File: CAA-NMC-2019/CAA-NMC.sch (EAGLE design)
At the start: 147 parts, among them IC1 ATTINY85-20SU, J1 M20-9980346

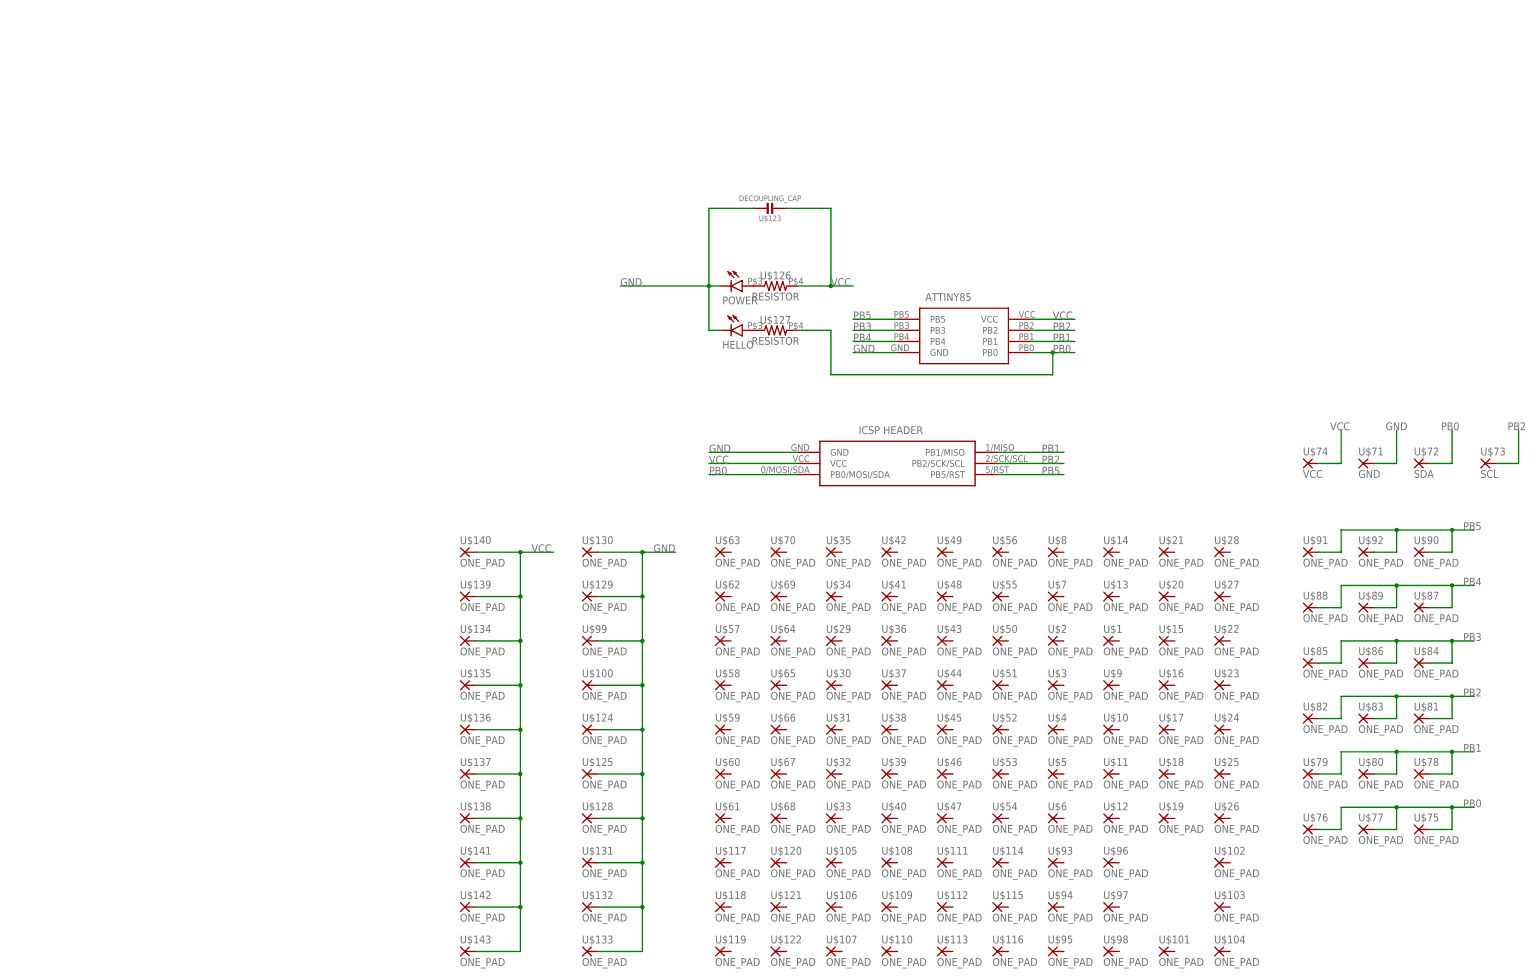
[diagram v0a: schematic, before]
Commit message: added smt battery mount
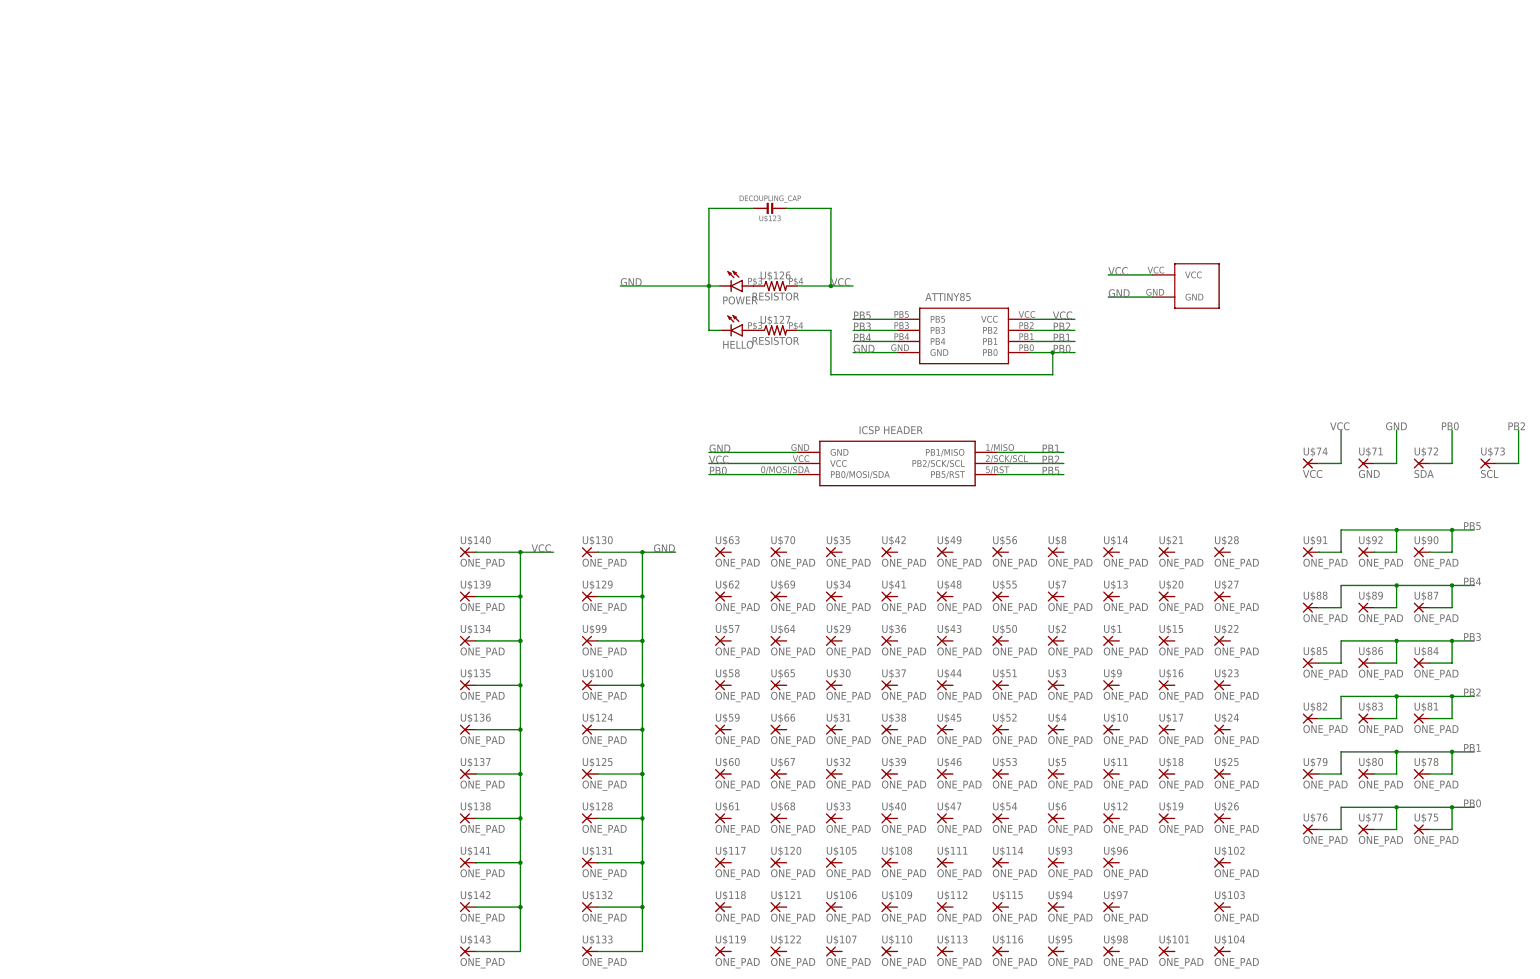
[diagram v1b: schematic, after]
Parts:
- added U$144: SMT-BATTERY-HOLDER, BadgeParts:SMT-BATTERY-HOLDER
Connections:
- net GND: now also U$144.GND
- net VCC: now also U$144.VCC

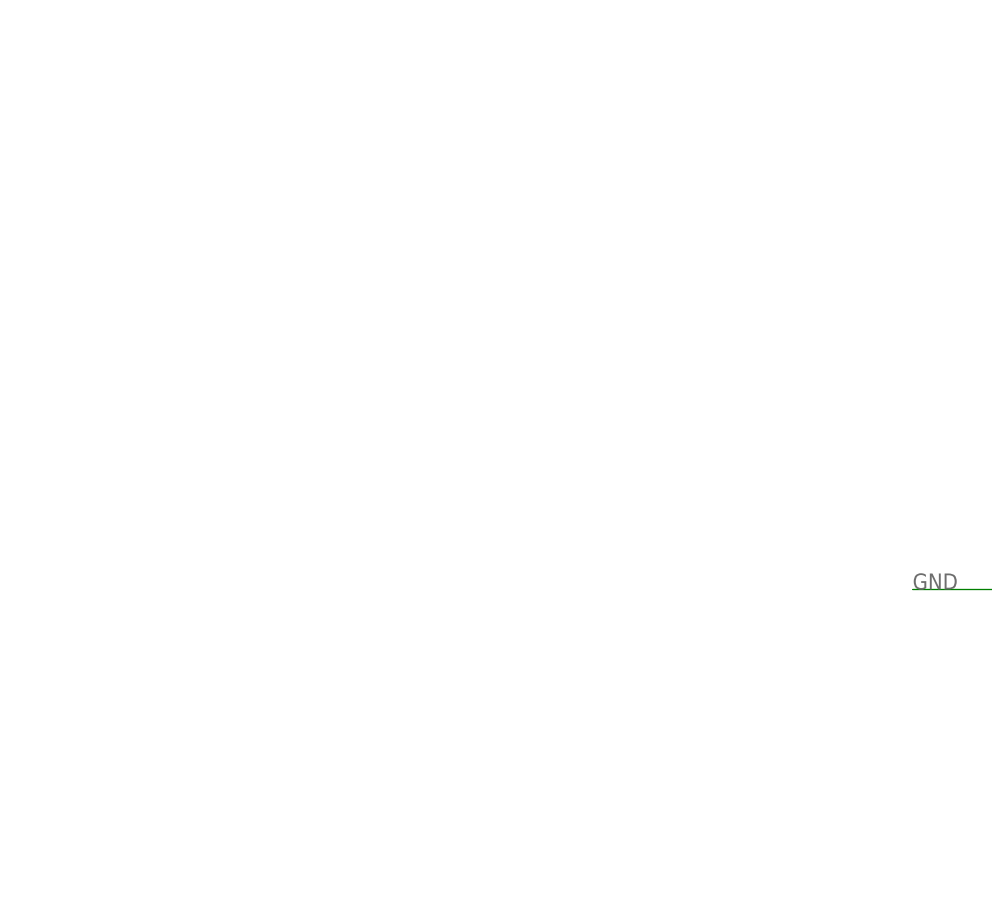
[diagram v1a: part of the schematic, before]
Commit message: added lanyard hole, 3 RGB LEDs
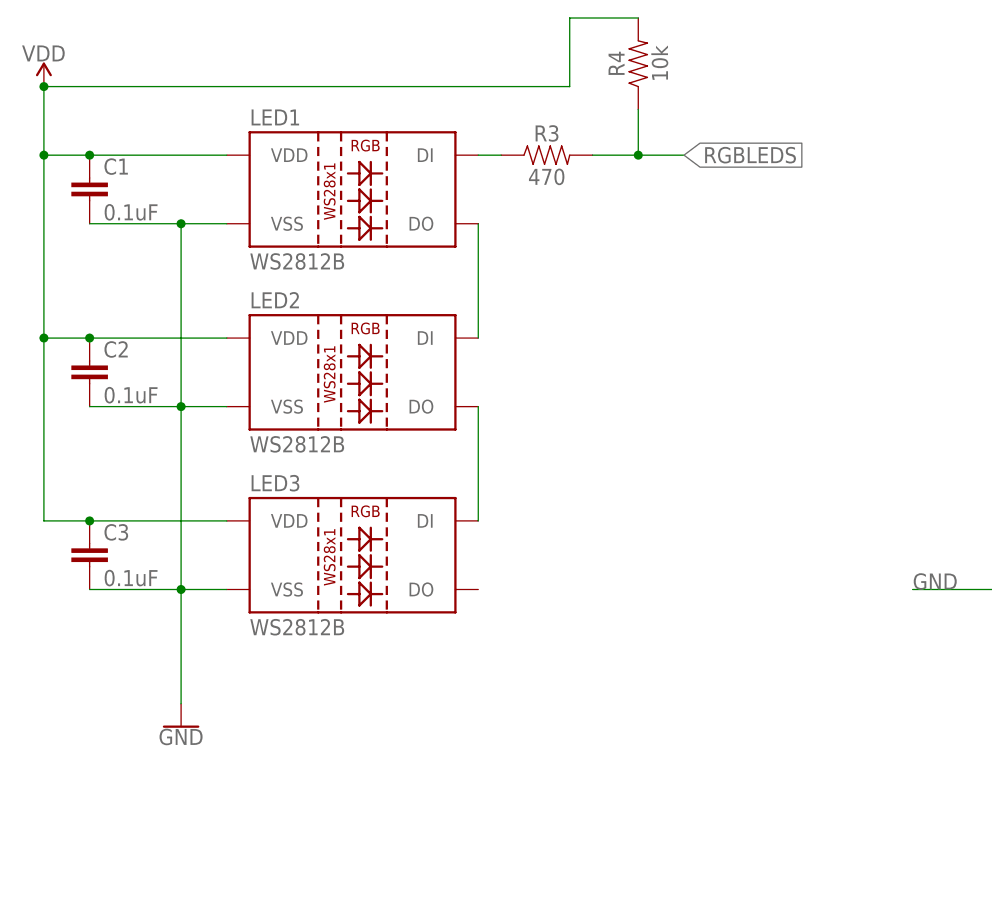
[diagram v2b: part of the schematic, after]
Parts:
- added C1, C2, C3: 0.1uF, SparkFun-Capacitors:0.1UF-0603-25V-5%
- added LED1, LED2, LED3: WS2812B, SparkFun-LED:WS2812B
- added R3: 470, SparkFun-Resistors:470OHM-0603-1/10W-1%
- added R4: 10k, SparkFun-Resistors:10KOHM-0603-1/10W-1%
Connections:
- new net N$10: LED2.DO, LED3.DI
- new net N$12: LED1.DI, R3.1
- new net N$9: LED1.DO, LED2.DI
- new net RGBLEDS: R3.2, R4.1
- new net VDD: C1.1, C2.1, C3.1, LED1.VDD, LED2.VDD, LED3.VDD, R4.2
- net GND: now also C1.2, C2.2, C3.2, LED1.VSS, LED2.VSS, LED3.VSS
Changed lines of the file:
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@@
 <part name="U$143" library="BadgeParts" deviceset="ONE_PAD" device=""/>
 <part name="U$144" library="BadgeParts" deviceset="SMT-BATTERY-HOLDER" device=""/>
+<part name="LED1" library="SparkFun-LED" library_urn="urn:adsk.eagle:library:529" deviceset="WS2812B" device="" package3d_urn="urn:adsk.eagle:package:39369/1" value="WS2812B"/>
+<part name="SUPPLY5" library="SparkFun-PowerSymbols" library_urn="urn:adsk.eagle:library:530" deviceset="VDD" device=""/>
+<part name="LED2" library="SparkFun-LED" library_urn="urn:adsk.eagle:library:529" deviceset="WS2812B" device="" package3d_urn="urn:adsk.eagle:package:39369/1" value="WS2812B"/>
+<part name="LED3" library="SparkFun-LED" library_urn="urn:adsk.eagle:library:529" deviceset="WS2812B" device="" package3d_urn="urn:adsk.eagle:package:39369/1" value="WS2812B"/>
+<part name="C1" library="SparkFun-Capacitors" library_urn="urn:adsk.eagle:library:510" deviceset="0.1UF" device="-0603-25V-5%" package3d_urn="urn:adsk.eagle:package:37414/1" value="0.1uF"/>
+<part name="C2" library="SparkFun-Capacitors" library_urn="urn:adsk.eagle:library:510" deviceset="0.1UF" device="-0603-25V-5%" package3d_urn="urn:adsk.eagle:package:37414/1" value="0.1uF"/>
+<part name="C3" library="SparkFun-Capacitors" library_urn="urn:adsk.eagle:library:510" deviceset="0.1UF" device="-0603-25V-5%" package3d_urn="urn:adsk.eagle:package:37414/1" value="0.1uF"/>
+<part name="R3" library="SparkFun-Resistors" library_urn="urn:adsk.eagle:library:532" deviceset="470OHM" device="-0603-1/10W-1%" package3d_urn="urn:adsk.eagle:package:39650/1" value="470"/>
+<part name="R4" library="SparkFun-Resistors" library_urn="urn:adsk.eagle:library:532" deviceset="10KOHM" device="-0603-1/10W-1%" package3d_urn="urn:adsk.eagle:package:39650/1" value="10k"/>
+<part name="GND5" library="SparkFun-PowerSymbols" library_urn="urn:adsk.eagle:library:530" deviceset="GND" device=""/>
 </parts>
 <sheets>
@@
 </instance>
 <instance part="U$144" gate="G$1" x="-55.88" y="76.2" smashed="yes"/>
+<instance part="LED1" gate="G$1" x="-243.84" y="116.84" smashed="yes">
+<attribute name="NAME" x="-256.54" y="125.222" size="1.778" layer="95"/>
+<attribute name="VALUE" x="-256.54" y="109.22" size="1.778" layer="95"/>
+</instance>
+<instance part="SUPPLY5" gate="VDD" x="-279.4" y="129.54" smashed="yes">
+<attribute name="VALUE" x="-279.4" y="132.334" size="1.778" layer="96" align="bottom-center"/>
+</instance>
+<instance part="LED2" gate="G$1" x="-243.84" y="96.52" smashed="yes">
+<attribute name="NAME" x="-256.54" y="104.902" size="1.778" layer="95"/>
+<attribute name="VALUE" x="-256.54" y="88.9" size="1.778" layer="95"/>
+</instance>
+<instance part="LED3" gate="G$1" x="-243.84" y="76.2" smashed="yes">
+<attribute name="NAME" x="-256.54" y="84.582" size="1.778" layer="95"/>
+<attribute name="VALUE" x="-256.54" y="68.58" size="1.778" layer="95"/>
+</instance>
+<instance part="C1" gate="G$1" x="-274.32" y="116.84" smashed="yes">
+<attribute name="NAME" x="-272.796" y="119.761" size="1.778" layer="95" font="vector"/>
+<attribute name="VALUE" x="-272.796" y="114.681" size="1.778" layer="96" font="vector"/>
+</instance>
+<instance part="C2" gate="G$1" x="-274.32" y="96.52" smashed="yes">
+<attribute name="NAME" x="-272.796" y="99.441" size="1.778" layer="95" font="vector"/>
+<attribute name="VALUE" x="-272.796" y="94.361" size="1.778" layer="96" font="vector"/>
+</instance>
+<instance part="C3" gate="G$1" x="-274.32" y="76.2" smashed="yes">
+<attribute name="NAME" x="-272.796" y="79.121" size="1.778" layer="95" font="vector"/>
+<attribute name="VALUE" x="-272.796" y="74.041" size="1.778" layer="96" font="vector"/>
+</instance>
+<instance part="R3" gate="G$1" x="-223.52" y="121.92" smashed="yes">
+<attribute name="NAME" x="-223.52" y="123.444" size="1.778" layer="95" font="vector" align="bottom-center"/>
+<attribute name="VALUE" x="-223.52" y="120.396" size="1.778" layer="96" font="vector" align="top-center"/>
+</instance>
+<instance part="R4" gate="G$1" x="-213.36" y="132.08" smashed="yes" rot="R90">
+<attribute name="NAME" x="-214.884" y="132.08" size="1.778" layer="95" font="vector" rot="R90" align="bottom-center"/>
+<attribute name="VALUE" x="-211.836" y="132.08" size="1.778" layer="96" font="vector" rot="R90" align="top-center"/>
+</instance>
+<instance part="GND5" gate="1" x="-264.16" y="58.42" smashed="yes">
+<attribute name="VALUE" x="-264.16" y="58.166" size="1.778" layer="96" align="top-center"/>
+</instance>
 </instances>
 <busses>
@@
 <label x="-71.12" y="71.12" size="1.778" layer="95"/>
 </segment>
+<segment>
+<pinref part="LED3" gate="G$1" pin="VSS"/>
+<pinref part="C3" gate="G$1" pin="2"/>
+<wire x1="-259.08" y1="73.66" x2="-264.16" y2="73.66" width="0.1524" layer="91"/>
+<wire x1="-264.16" y1="73.66" x2="-274.32" y2="73.66" width="0.1524" layer="91"/>
+<junction x="-264.16" y="73.66"/>
+<pinref part="LED2" gate="G$1" pin="VSS"/>
+<pinref part="C2" gate="G$1" pin="2"/>
+<wire x1="-259.08" y1="93.98" x2="-264.16" y2="93.98" width="0.1524" layer="91"/>
+<wire x1="-264.16" y1="93.98" x2="-274.32" y2="93.98" width="0.1524" layer="91"/>
+<wire x1="-264.16" y1="73.66" x2="-264.16" y2="93.98" width="0.1524" layer="91"/>
+<junction x="-264.16" y="93.98"/>
+<pinref part="LED1" gate="G$1" pin="VSS"/>
+<pinref part="C1" gate="G$1" pin="2"/>
+<wire x1="-259.08" y1="114.3" x2="-264.16" y2="114.3" width="0.1524" layer="91"/>
+<wire x1="-264.16" y1="114.3" x2="-274.32" y2="114.3" width="0.1524" layer="91"/>
+<wire x1="-264.16" y1="93.98" x2="-264.16" y2="114.3" width="0.1524" layer="91"/>
+<junction x="-264.16" y="114.3"/>
+<pinref part="GND5" gate="1" pin="GND"/>
+<wire x1="-264.16" y1="73.66" x2="-264.16" y2="60.96" width="0.1524" layer="91"/>
+</segment>
 </net>
 <net name="PB2" class="0">
@@
 </segment>
 </net>
+<net name="VDD" class="1">
+<segment>
+<pinref part="LED1" gate="G$1" pin="VDD"/>
+<pinref part="C1" gate="G$1" pin="1"/>
+<wire x1="-259.08" y1="121.92" x2="-274.32" y2="121.92" width="0.1524" layer="91"/>
+<pinref part="SUPPLY5" gate="VDD" pin="VDD"/>
+<wire x1="-274.32" y1="121.92" x2="-279.4" y2="121.92" width="0.1524" layer="91"/>
+<wire x1="-279.4" y1="121.92" x2="-279.4" y2="129.54" width="0.1524" layer="91"/>
+<junction x="-274.32" y="121.92"/>
+<pinref part="LED2" gate="G$1" pin="VDD"/>
+<pinref part="C2" gate="G$1" pin="1"/>
+<wire x1="-259.08" y1="101.6" x2="-274.32" y2="101.6" width="0.1524" layer="91"/>
+<wire x1="-274.32" y1="101.6" x2="-279.4" y2="101.6" width="0.1524" layer="91"/>
+<wire x1="-279.4" y1="101.6" x2="-279.4" y2="121.92" width="0.1524" layer="91"/>
+<junction x="-274.32" y="101.6"/>
+<junction x="-279.4" y="121.92"/>
+<pinref part="LED3" gate="G$1" pin="VDD"/>
+<pinref part="C3" gate="G$1" pin="1"/>
+<wire x1="-259.08" y1="81.28" x2="-274.32" y2="81.28" width="0.1524" layer="91"/>
+<wire x1="-274.32" y1="81.28" x2="-279.4" y2="81.28" width="0.1524" layer="91"/>
+<wire x1="-279.4" y1="81.28" x2="-279.4" y2="101.6" width="0.1524" layer="91"/>
+<junction x="-274.32" y="81.28"/>
+<junction x="-279.4" y="101.6"/>
+<wire x1="-279.4" y1="129.54" x2="-220.98" y2="129.54" width="0.1524" layer="91"/>
+<junction x="-279.4" y="129.54"/>
+<wire x1="-220.98" y1="129.54" x2="-220.98" y2="137.16" width="0.1524" layer="91"/>
+<pinref part="R4" gate="G$1" pin="2"/>
+<wire x1="-220.98" y1="137.16" x2="-213.36" y2="137.16" width="0.1524" layer="91"/>
+</segment>
+</net>
+<net name="RGBLEDS" class="0">
+<segment>
+<pinref part="R3" gate="G$1" pin="2"/>
+<wire x1="-218.44" y1="121.92" x2="-213.36" y2="121.92" width="0.1524" layer="91"/>
+<pinref part="R4" gate="G$1" pin="1"/>
+<wire x1="-213.36" y1="127" x2="-213.36" y2="121.92" width="0.1524" layer="91"/>
+<wire x1="-213.36" y1="121.92" x2="-208.28" y2="121.92" width="0.1524" layer="91"/>
+<junction x="-213.36" y="121.92"/>
+<label x="-208.28" y="121.92" size="1.778" layer="95" xref="yes"/>
+</segment>
+</net>
+<net name="N$9" class="0">
+<segment>
+<pinref part="LED1" gate="G$1" pin="DO"/>
+<pinref part="LED2" gate="G$1" pin="DI"/>
+<wire x1="-231.14" y1="114.3" x2="-231.14" y2="101.6" width="0.1524" layer="91"/>
+</segment>
+</net>
+<net name="N$10" class="0">
+<segment>
+<pinref part="LED2" gate="G$1" pin="DO"/>
+<pinref part="LED3" gate="G$1" pin="DI"/>
+<wire x1="-231.14" y1="93.98" x2="-231.14" y2="81.28" width="0.1524" layer="91"/>
+</segment>
+</net>
+<net name="N$12" class="0">
+<segment>
+<pinref part="LED1" gate="G$1" pin="DI"/>
+<pinref part="R3" gate="G$1" pin="1"/>
+<wire x1="-231.14" y1="121.92" x2="-228.6" y2="121.92" width="0.1524" layer="91"/>
+</segment>
+</net>
 </nets>
 </sheet>
@@
 which will not be processed correctly with this version.
 </note>
+<note version="8.2" severity="warning">
+Since Version 8.2, EAGLE supports online libraries. The ids
+of those online libraries will not be understood (or retained)
+with this version.
+</note>
 <note version="8.3" severity="warning">
 Since Version 8.3, EAGLE supports URNs for individual library
@@
 will not be understood (or retained) with this version.
 </note>
+<note version="8.3" severity="warning">
+Since Version 8.3, EAGLE supports the association of 3D packages
+with devices in libraries, schematics, and board files. Those 3D
+packages will not be understood (or retained) with this version.
+</note>
 </compatibility>
